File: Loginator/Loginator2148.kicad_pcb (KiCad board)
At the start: 2 copper layers, 61 x 38.1 mm, 66 parts, among them J001 USBSMD, J002 M01PTH, J301 JST 2mm, J401 M06, J402 M04, J403 M10, J404 M06, J406 11DoF, Q050 PMOS, Q201 PMOS, U201 5319, U202 4173, U301 73831, U401 LPC2148, U402 1525, U701 MICROSD-SOCKET, Y401 12M

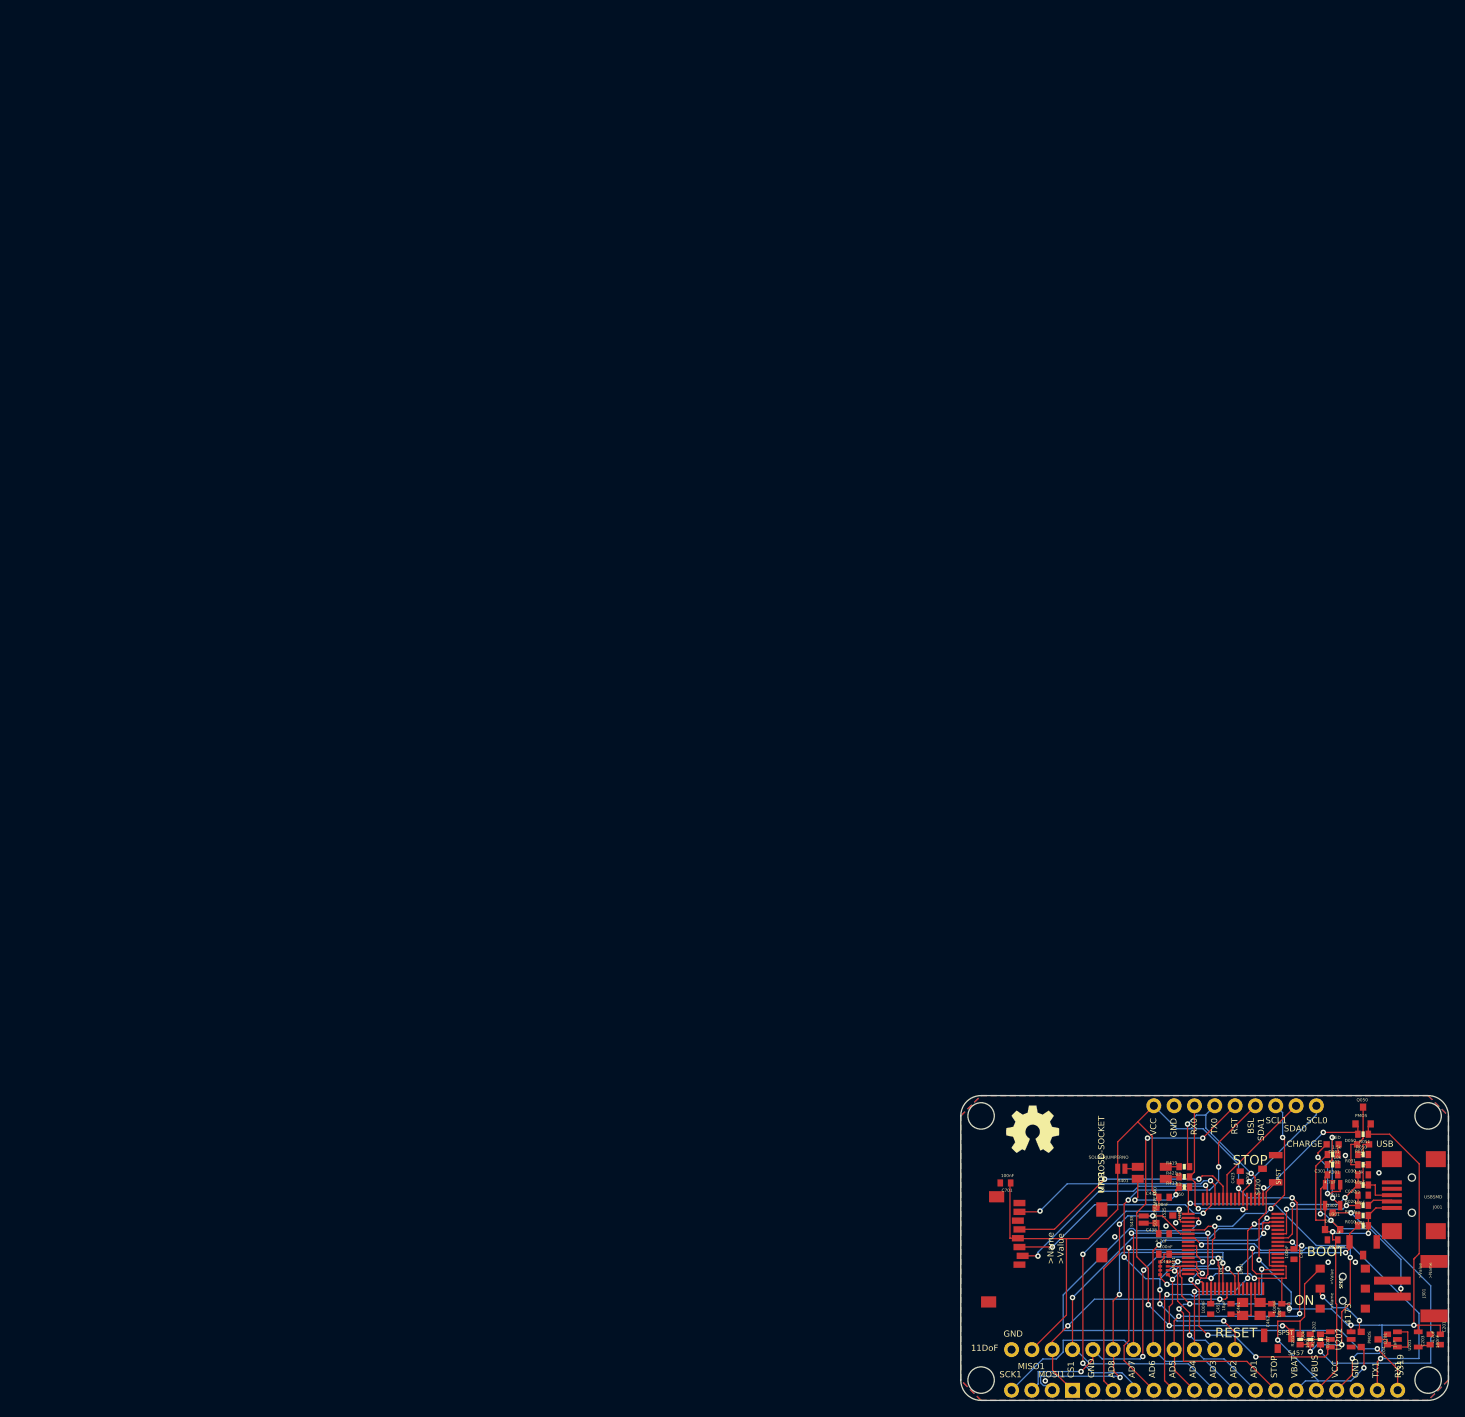
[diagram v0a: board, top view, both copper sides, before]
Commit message: Loginator schematic and board are now consistent
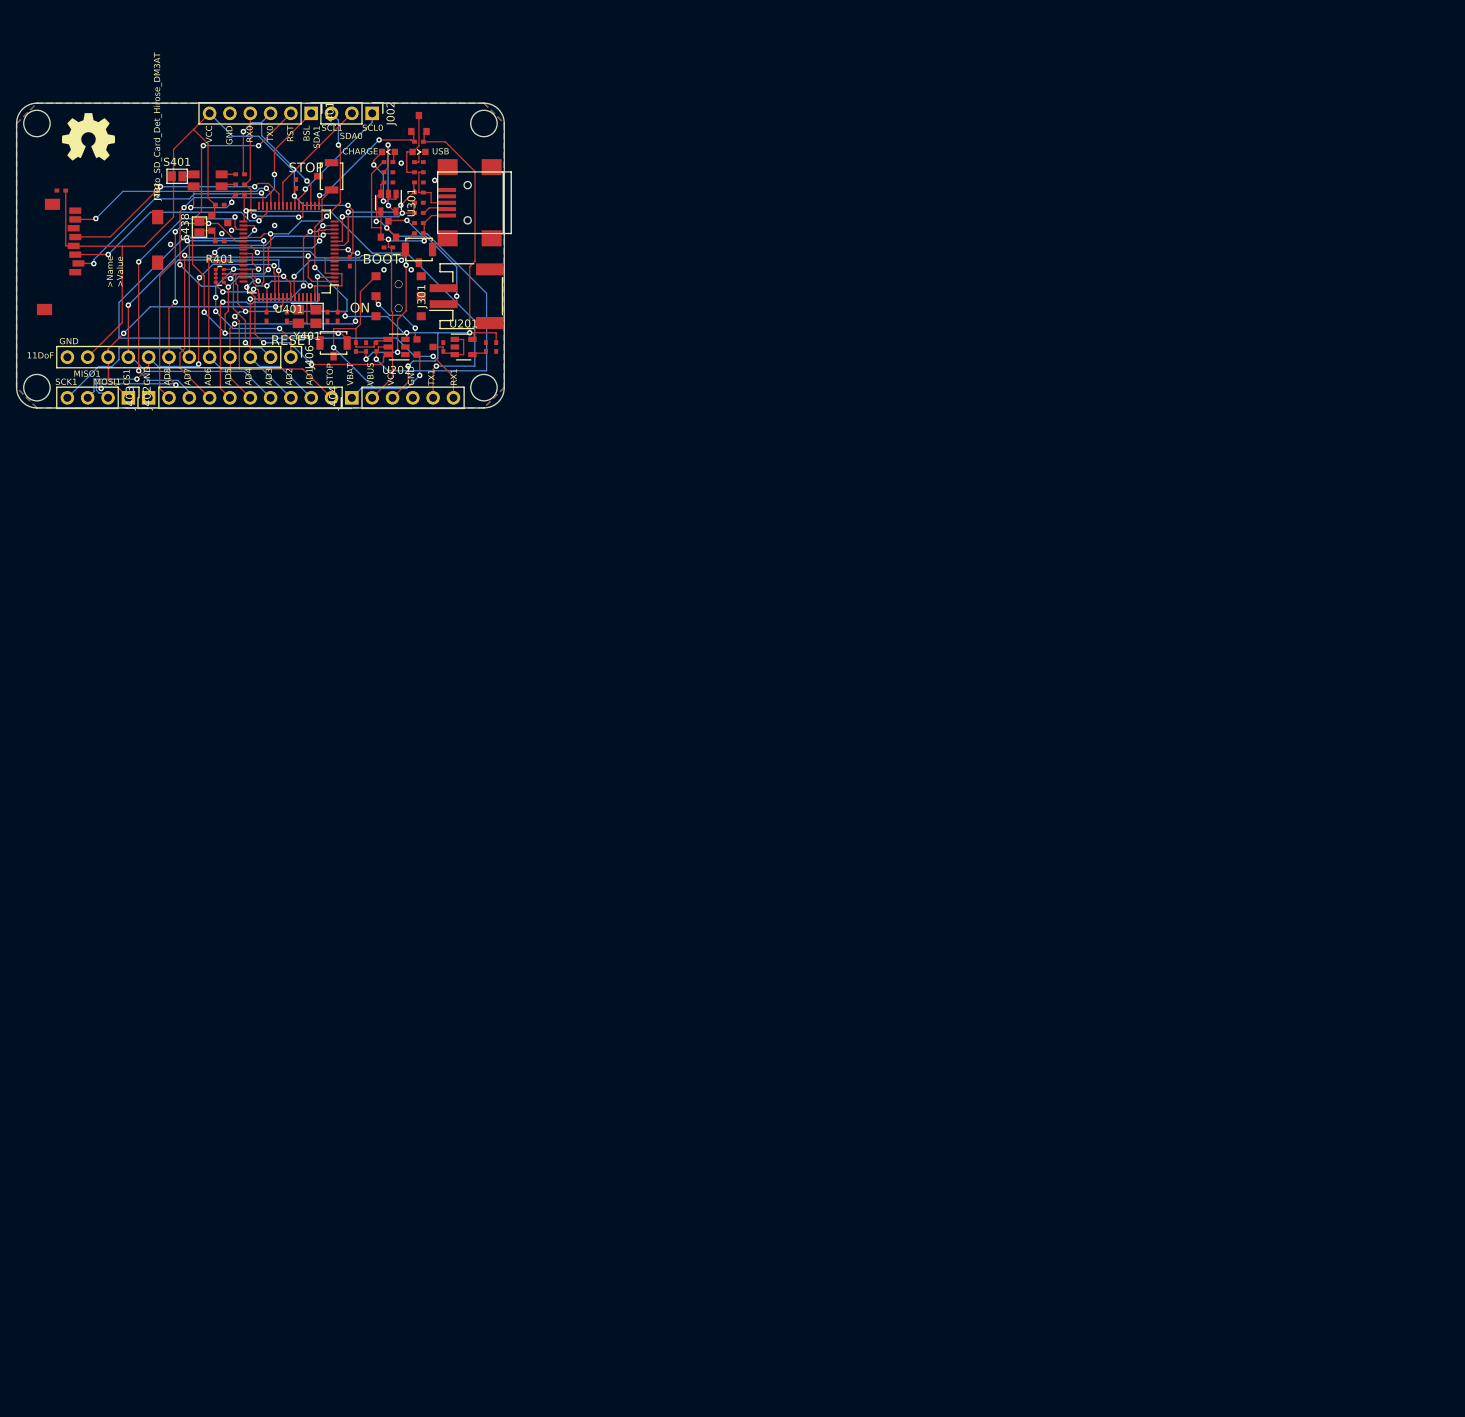
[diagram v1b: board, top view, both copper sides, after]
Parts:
- removed U701: MICROSD-SOCKET, MICROSD-SOCKET-PP
- added J701: Micro_SD_Card_Det_Hirose_DM3AT, KwanSystems:MICROSD-SOCKET-PP, F.Cu at (18.0, -25.9)
- C020, C030, C203, C204, C301, C302, C407, C423, C432, C438, C443, C451, C461, C462, C463, C701: footprint 0402-CAP -> KwanSystems:SMD_0402
- C201: value 4.7uF -> 4.7nF; footprint 0402-CAP -> KwanSystems:SMD_0402
- D050, D301: footprint LED-0603 -> KwanSystems:D_0603
- D302, U402: footprint SOT-23-3 -> KwanSystems:SOT-23
- D401: footprint HSMF-C118 -> KwanSystems:HSMF-C118
- J001: value USBSMD -> USB_MICROB; footprint USB-MINIB -> KwanSystems:USB_Mini-B
- J002: footprint 1X03 -> Pin_Headers:Pin_Header_Straight_1x03_Pitch2.54mm
- J301: footprint JST-2-SMD -> Connectors_JST:JST_PH_S2B-PH-SM4-TB_02x2.00mm_Angled
- J401, J404: footprint 1X06 -> Pin_Headers:Pin_Header_Straight_1x06_Pitch2.54mm
- J402: footprint 1X04 -> Pin_Headers:Pin_Header_Straight_1x04_Pitch2.54mm
- J403: footprint 1X10 -> Pin_Headers:Pin_Header_Straight_1x10_Pitch2.54mm
- J406: footprint 1X12 -> Pin_Headers:Pin_Header_Straight_1x12_Pitch2.54mm
- Q050, Q201: footprint SOT23-3 -> KwanSystems:SOT-23
- R010, R011, R020, R030, R031, R050, R051, R201, R202, R203, R301, R302, R419, R421, R433: footprint 0402-RES -> KwanSystems:SMD_0402
- R401: footprint CRA04 -> KwanSystems:R_Array_Convex_4x0402
- S010, S420, S457: footprint B3U-1100P -> KwanSystems:SW_SPST_B3U-1100P
- S201: footprint AYZ0202 -> KwanSystems:SWITCH_DPDT_AZY0202
- S401, S438: value SOLDERJUMPERNO -> GS2; footprint SJ_2S-NO -> Connectors:GS2
- U201: value 5319 -> MIC5319; footprint SOT-23-5 -> TO_SOT_Packages_SMD:SOT-23-5
- U202: value 4173 -> MAX4173; footprint SOT-23-6 -> TO_SOT_Packages_SMD:SOT-23-6
- U301: value 73831 -> MCP73831; footprint SOT23-5 -> TO_SOT_Packages_SMD:SOT-23-5
- U401: footprint SQFP-S-10X10-64 -> Housings_QFP:LQFP-64_10x10mm_Pitch0.5mm
- Y401: value 12M -> 12MHz; footprint CRYSTAL_SMD -> Crystals:Crystal_SMD_Abracon_ABM8G-4pin_3.2x2.5mm
- moved J301 172.2 mm to (56.3, -14.0), turned to 90 degrees
- moved C462 171.2 mm to (38.9, -11.4)
- moved J406 171.2 mm to (34.3, -6.35), turned to 270 degrees
- moved C020 171.2 mm to (50.3, -25.7)
- moved C030 171.2 mm to (50.3, -28.2)
- moved C201 171.2 mm to (59.9, -7.62)
- moved C203 171.2 mm to (58.7, -7.62)
- moved C204 171.2 mm to (53.3, -7.62)
- moved C301 171.2 mm to (46.5, -28.2)
- moved C302 171.2 mm to (46.5, -20.1)
- moved C407 171.2 mm to (41.7, -18.3)
- moved C423 171.2 mm to (34.9, -28.0)
- moved C432 171.2 mm to (25.4, -25.4)
- moved C438 171.2 mm to (25.4, -20.8)
- moved C443 171.2 mm to (25.4, -18.3)
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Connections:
- net AD1 renamed /AD1
- net AD2 renamed /AD2
- net AD3 renamed /AD3
- net AD4 renamed /AD4
- net AD5 renamed /AD5
- net AD6 renamed /AD6
- net AD7 renamed /AD7
- net ADREF+ renamed /ADREF+
- net ADREF- renamed /ADREF-
- net CURRENT renamed /CURRENT
- net N$10 renamed /N$10
- net N$17 renamed /N$17
- net N$2 renamed /N$2
- net RAW renamed /RAW
- net RX1 renamed /RX1
- net SCL0 renamed /SCL0
- net SCL1 renamed /SCL1
- net SDA0 renamed /SDA0
- net SDA1/BSL renamed /SDA1(BSL)
- net USBD+ renamed /USBD+
- net USBD- renamed /USBD-
- net USB_SOFTCONNECT renamed /USB_SOFTCONNECT
- net VIN+ renamed /VIN+
- C301 pad 1: VLIPO -> /VLIPO
- C302 pad 1: VBUS -> /VBUS
- C461 pad 2: XTAL2 -> /XTAL2
- C462 pad 2: XTAL1 -> /XTAL1
- D302 pad 1: VBUS -> /VBUS
- D302 pad 2: VLIPO -> /VLIPO
- D401 pad 1: RGB_Q -> /RGB_Q
- D401 pad 2: DR -> /DR
- D401 pad 3: DG -> /DG
- D401 pad 4: DB -> /DB
- J301 pad 1: GND -> /VLIPO
- J301 pad 2: VLIPO -> GND
- J401 pad 2: RST -> /RST
- J401 pad 3: TX0/PWMB -> /TX0(PWMB)
- J401 pad 4: RX0/PWMG -> /RX0(PWMG)
- J402 pad 1: CS1 -> /SCK1
- J402 pad 2: MOSI1 -> /MISO1
- J402 pad 3: MISO1 -> /MOSI1
- J402 pad 4: SCK1 -> /CS1
- J403 pad 10: STOP -> /STOP
- J404 pad 1: VIN- -> /VIN-
- J404 pad 2: VBUS -> /VBUS
- J404 pad 5: TX1/PWMR -> /TX1(PWMR)
- J406 pad 10: CS1 -> /CS1
- J406 pad 6: SCK1 -> /SCK1
- J406 pad 7: MOSI1 -> /MOSI1
- J406 pad 8: MISO1 -> /MISO1
- Q050 pad 3: N$6 -> /N$6
- Q201 pad 2: VIN- -> /VIN-
- R010 pad 1: USB_ON -> /USB_ON
- R010 pad 2: VBUS -> /VBUS
- R011 pad 2: VBUS -> /VBUS
- R020 pad 2: CONN_D- -> /CONN_D-
- R030 pad 2: CONN_D+ -> /CONN_D+
- R031 pad 1: N$6 -> /N$6
- R031 pad 2: CONN_D+ -> /CONN_D+
- R050 pad 1: N$7 -> /N$7
- R201 pad 1: BATLVL -> /VIN-
- R201 pad 2: VIN- -> /BATLVL
- R202 pad 1: GND -> /BATLVL
- R202 pad 2: BATLVL -> GND
- R203 pad 2: VIN- -> /VIN-
- R302 pad 1: N$1 -> /VBUS
- R302 pad 2: VBUS -> /N$1
- R401 pad 5: RST -> /RST
- R401 pad 7: STOP -> /STOP
- R419 pad 1: DB -> /TX0(PWMB)
- R419 pad 2: TX0/PWMB -> /DB
- R421 pad 1: DG -> /RX0(PWMG)
- R421 pad 2: RX0/PWMG -> /DG
- R433 pad 1: DR -> /TX1(PWMR)
- R433 pad 2: TX1/PWMR -> /DR
- S201 pad 3: VIN- -> /VIN-
- S401 pad 1: RGB_Q -> VCC
- S401 pad 2: VCC -> /RGB_Q
- U202 pad 4: VIN- -> /VIN-
- U301 pad 1: N$3 -> /N$3
- U301 pad 3: VLIPO -> /VLIPO
- U301 pad 4: VBUS -> /VBUS
- U401 pad 19: TX0/PWMB -> /TX0(PWMB)
- U401 pad 21: RX0/PWMG -> /RX0(PWMG)
- U401 pad 27: SCK0 -> /SCK0
- U401 pad 29: MISO0 -> /MISO0
- U401 pad 30: MOSI0 -> /MOSI0
- U401 pad 31: CS0 -> /CS0
- U401 pad 33: TX1/PWMR -> /TX1(PWMR)
- U401 pad 39: BATLVL -> /BATLVL
- U401 pad 46: STOP -> /STOP
- U401 pad 47: SCK1 -> /SCK1
- U401 pad 53: MISO1 -> /MISO1
- U401 pad 54: MOSI1 -> /MOSI1
- U401 pad 55: CS1 -> /CS1
- U401 pad 57: RST -> /RST
- U401 pad 58: USB_ON -> /USB_ON
- U401 pad 61: XTAL2 -> /XTAL2
- U401 pad 62: XTAL1 -> /XTAL1
- Y401 pad 1: XTAL2 -> /XTAL1
- Y401 pad 3: XTAL1 -> /XTAL2
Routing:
- net RST: track 71.5 -> 0.00 mm, vias 7 -> 0
- net /RST: track 0.00 -> 71.5 mm, vias 0 -> 7
- net /STOP: track 0.00 -> 59.6 mm, vias 0 -> 3
- net STOP: track 59.6 -> 0.00 mm, vias 3 -> 0
- net /MOSI1: track 0.00 -> 55.0 mm, vias 0 -> 4
- net TX1/PWMR: track 52.6 -> 0.00 mm, vias 2 -> 0
- net /TX1(PWMR): track 0.00 -> 52.6 mm, vias 0 -> 2
- net SCK1: track 52.0 -> 0.00 mm, vias 2 -> 0
- net VBUS: track 46.4 -> 0.00 mm, vias 2 -> 0
- net /VBUS: track 0.00 -> 46.4 mm, vias 0 -> 2
- net /CS1: track 0.00 -> 46.4 mm, vias 0 -> 2
- net MOSI1: track 46.2 -> 0.00 mm, vias 3 -> 0
- net MISO1: track 43.0 -> 0.00 mm, vias 4 -> 0
- net /BATLVL: track 0.00 -> 40.2 mm, vias 0 -> 4
- net BATLVL: track 40.2 -> 0.00 mm, vias 4 -> 0
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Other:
- net class Default: trace_width 0.25 -> 0.1524; via_dia 0.8 -> 0.508; via_drill 0.4 -> 0.254
- rule pad_to_mask_clearance: 0.2 -> 0
- rule via_min_drill: 0.3 -> 0.254
- rule via_min_size: 0.4 -> 0.508

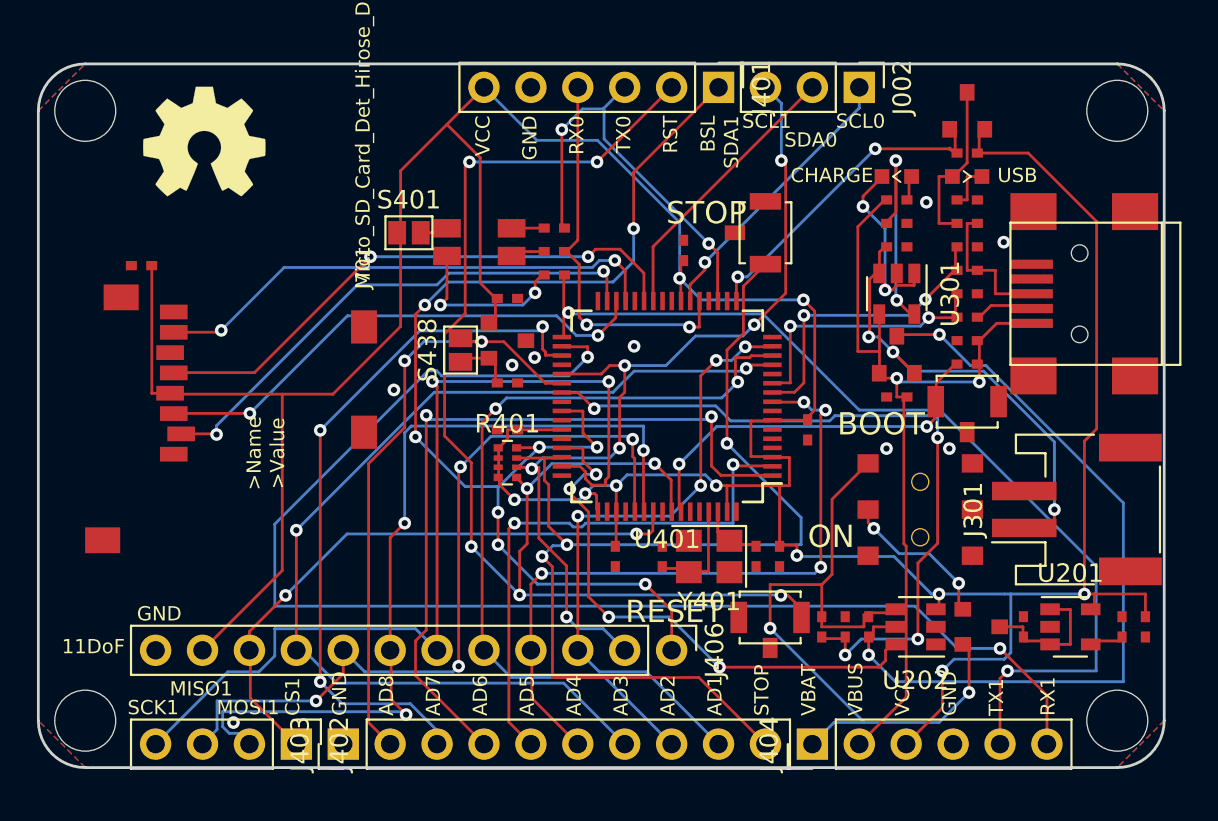
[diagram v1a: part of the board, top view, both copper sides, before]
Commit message: Consistent board and schematic, which passes ERC and DRC
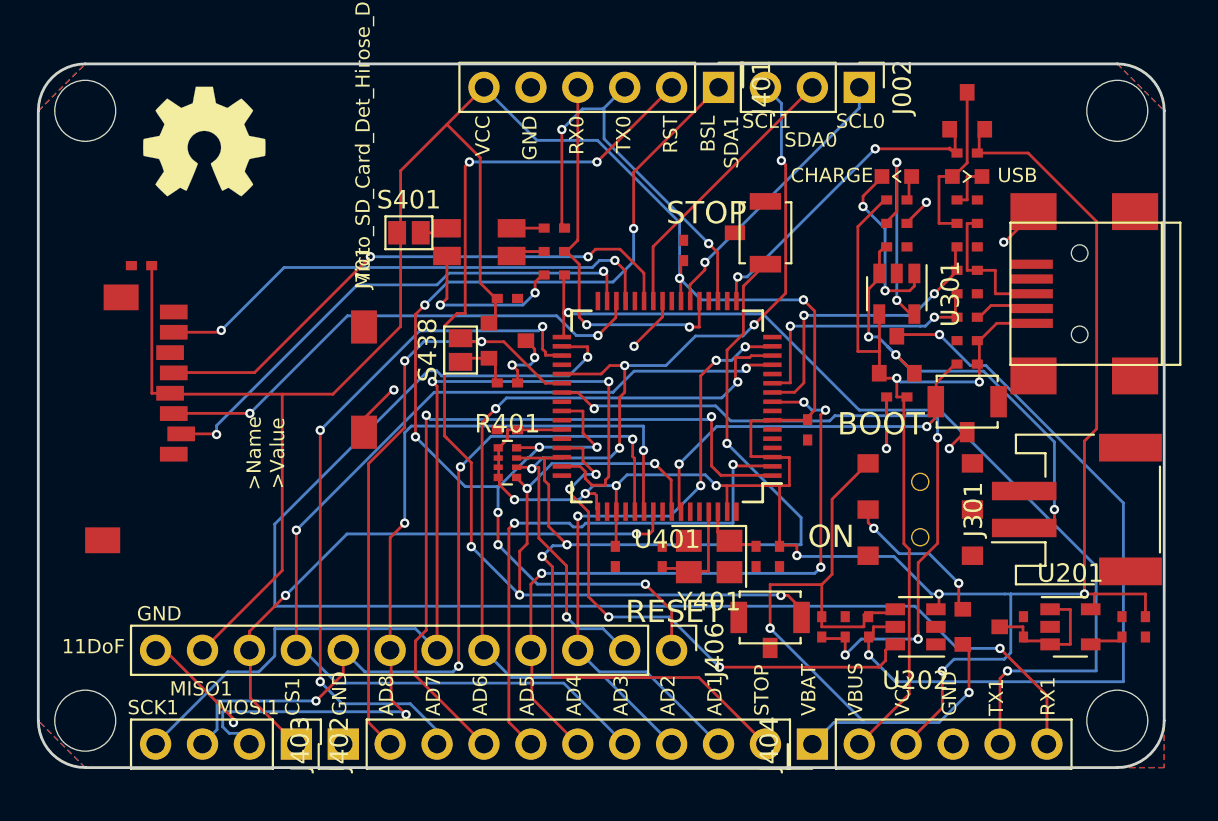
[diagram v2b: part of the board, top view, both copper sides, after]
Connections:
- J001 pad 4: (no net) -> Net-(J001-Pad4)
- J402 pad 1: /SCK1 -> /CS1
- J402 pad 2: /MISO1 -> /MOSI1
- J402 pad 3: /MOSI1 -> /MISO1
- J402 pad 4: /CS1 -> /SCK1
- J701 pad 1: (no net) -> Net-(J701-Pad1)
- J701 pad 10: (no net) -> Net-(J701-Pad10)
- J701 pad 8: (no net) -> Net-(J701-Pad8)
- U401 pad 12: (no net) -> Net-(U401-Pad12)
- U401 pad 16: (no net) -> Net-(U401-Pad16)
- U401 pad 20: (no net) -> Net-(U401-Pad20)
- U401 pad 24: (no net) -> Net-(U401-Pad24)
- U401 pad 28: (no net) -> Net-(U401-Pad28)
- U401 pad 32: (no net) -> Net-(U401-Pad32)
- U401 pad 36: (no net) -> Net-(U401-Pad36)
- U401 pad 4: (no net) -> Net-(U401-Pad4)
- U401 pad 40: (no net) -> Net-(U401-Pad40)
- U401 pad 44: (no net) -> Net-(U401-Pad44)
- U401 pad 48: (no net) -> Net-(U401-Pad48)
- U401 pad 5: (no net) -> Net-(U401-Pad5)
- U401 pad 52: (no net) -> Net-(U401-Pad52)
- U401 pad 56: (no net) -> Net-(U401-Pad56)
- U401 pad 60: (no net) -> Net-(U401-Pad60)
- U401 pad 64: (no net) -> Net-(U401-Pad64)
- U401 pad 8: (no net) -> Net-(U401-Pad8)
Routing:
- net GND: track 0.00 -> 26.2 mm, vias 0 -> 9
- net /CS1: track 46.4 -> 32.4 mm
- net /SCK1: track 38.0 -> 52.0 mm
- net /MOSI1: track 55.0 -> 46.2 mm, vias 4 -> 3
- net /MISO1: track 34.2 -> 43.0 mm, vias 3 -> 4
- net (no net): vias 9 -> 0
